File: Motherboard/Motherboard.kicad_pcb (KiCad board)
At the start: 4 copper layers, 246.4 x 175.3 mm, 57 parts, among them J1 40-pin IDE Connector, J3 Bus_ISA_8bit, J4 ATX-24, J5 USB_B, J6 ATF15XX_JTAG_ISP, J7 Bus_ISA_8bit, J8 65SIB_Connector, SW1 SW_Push, SW2 SW_SPST, U1 AS6C8008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

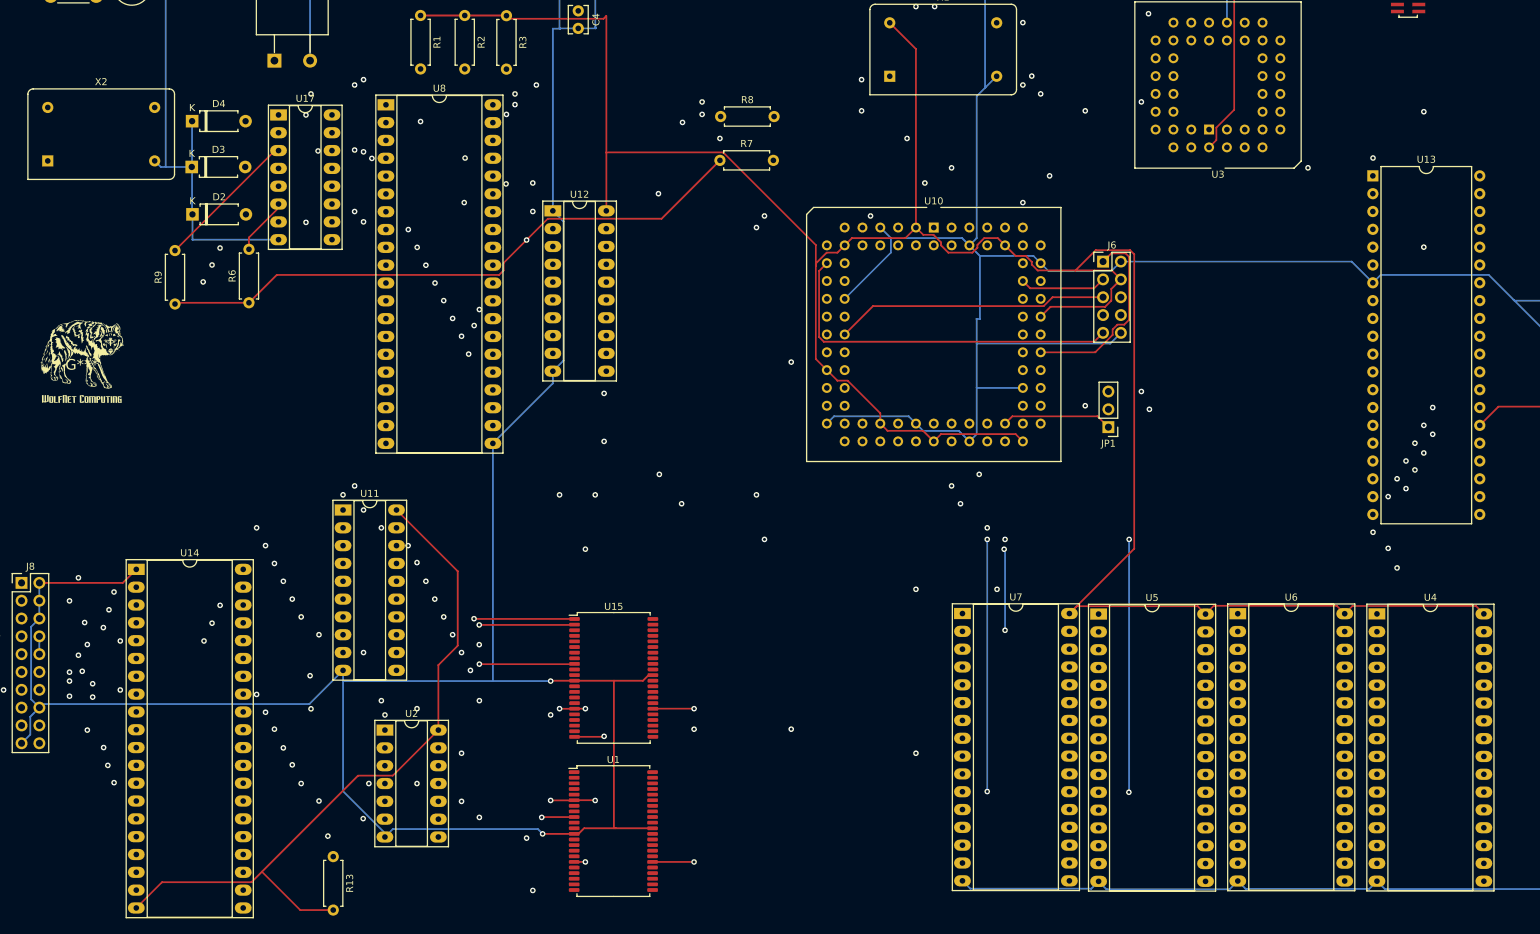
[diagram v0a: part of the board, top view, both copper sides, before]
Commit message: 230 unrouted traces...
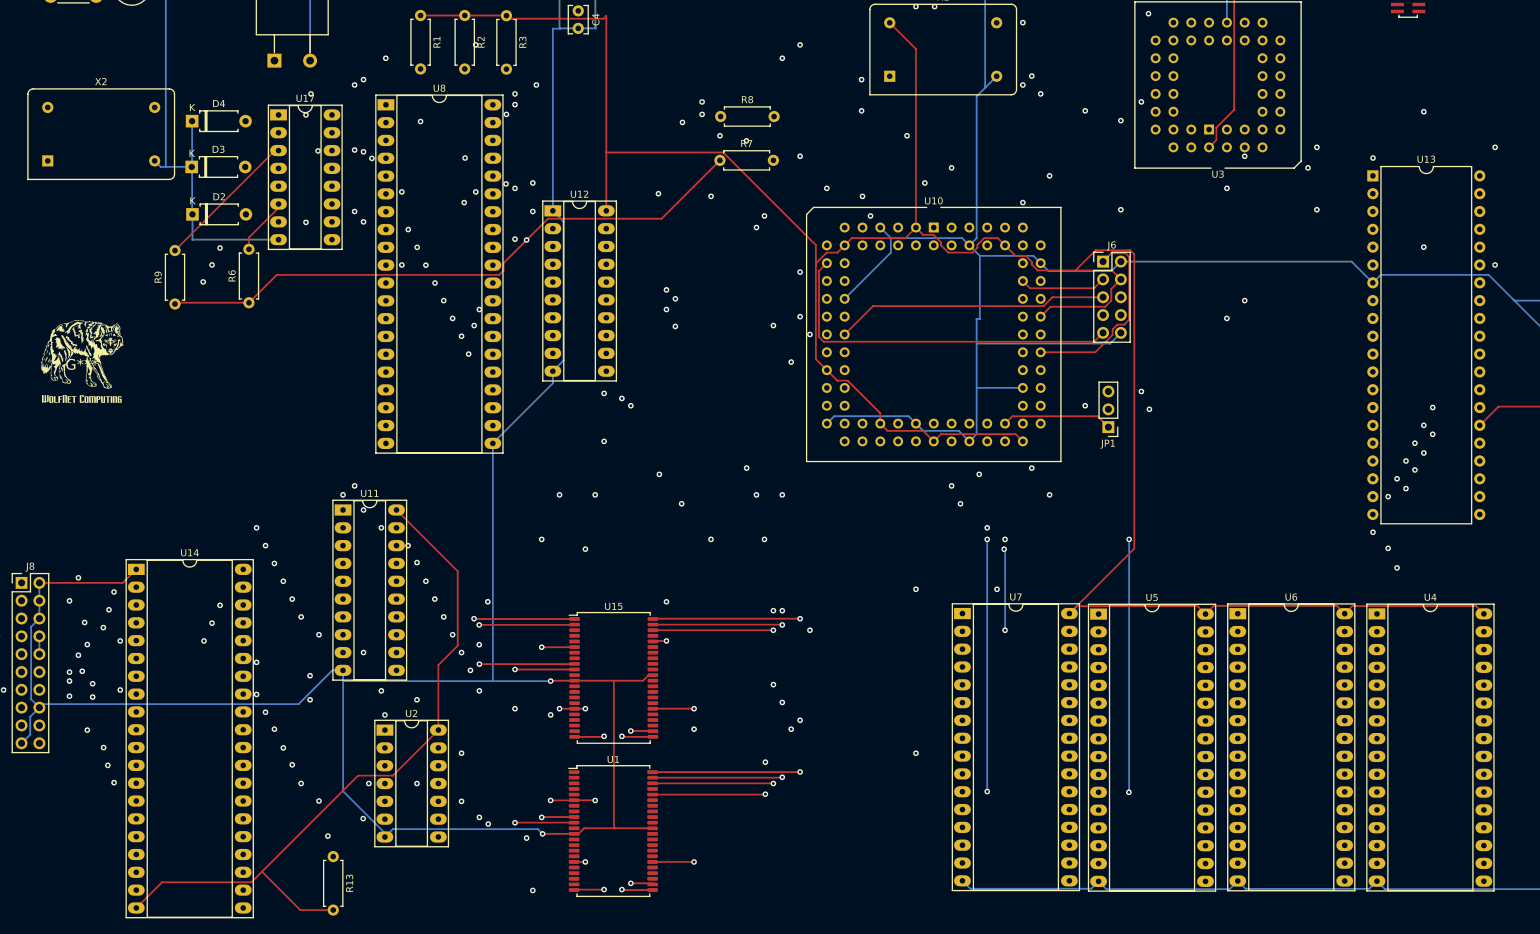
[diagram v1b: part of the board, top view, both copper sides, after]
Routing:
- net A1: track 142.2 -> 375.3 mm, vias 2 -> 11
- net A0: track 141.6 -> 323.3 mm, vias 2 -> 7
- net ~{VectorPull}: track 0.00 -> 174.2 mm, vias 0 -> 4
- net A6: track 62.1 -> 201.1 mm, vias 0 -> 6
- net A5: track 62.1 -> 196.0 mm, vias 0 -> 4
- net A7: track 62.3 -> 195.3 mm, vias 0 -> 5
- net Memory/IndexSelect: track 0.00 -> 130.4 mm, vias 0 -> 3
- net ~{RAM1_EN}: track 0.00 -> 119.1 mm, vias 0 -> 5
- net RESET: track 134.1 -> 236.0 mm, vias 5 -> 11
- net Net-(U15-CE2): track 0.00 -> 80.1 mm, vias 0 -> 4
- net A14: track 113.7 -> 192.5 mm, vias 0 -> 3
- net Net-(U1-CE2): track 0.00 -> 75.7 mm, vias 0 -> 2
- net D1: track 99.9 -> 174.4 mm, vias 2 -> 5
- net A13: track 109.9 -> 184.3 mm, vias 0 -> 3
- net A3: track 171.5 -> 226.9 mm, vias 3 -> 5
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
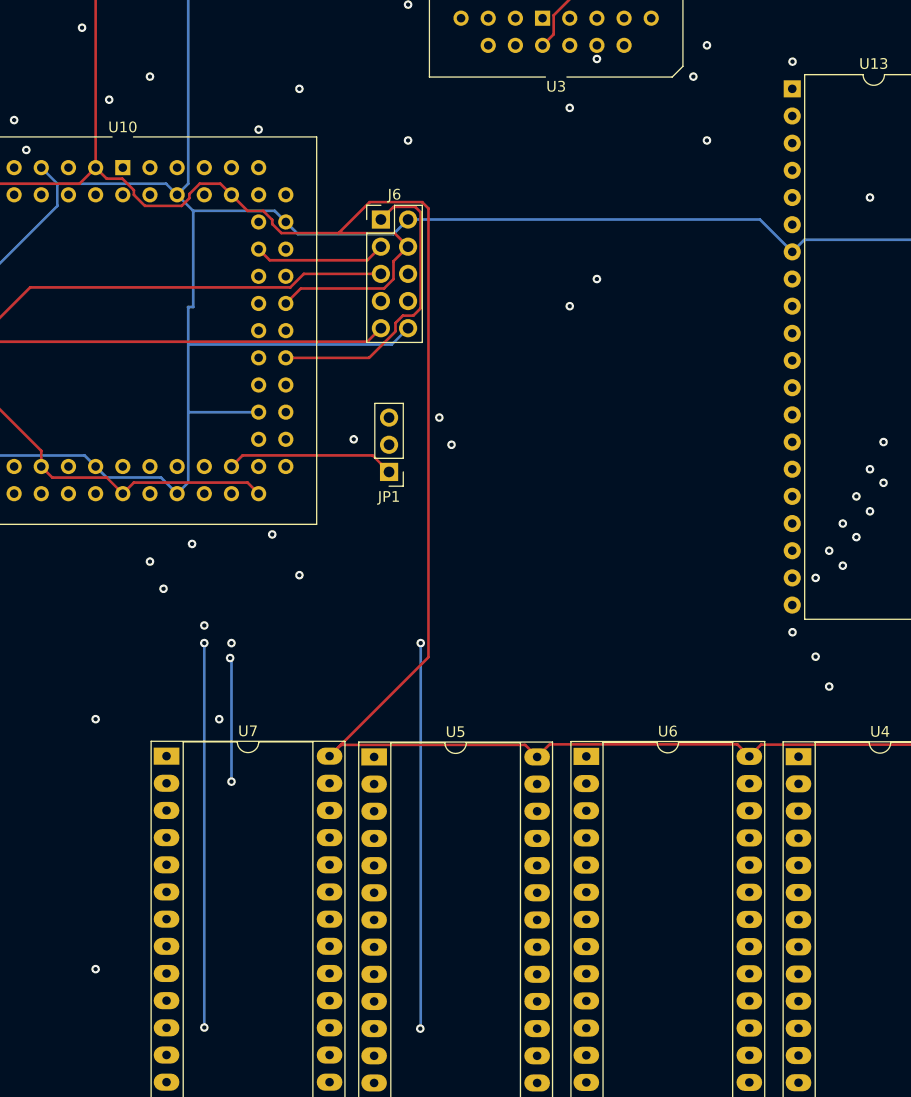
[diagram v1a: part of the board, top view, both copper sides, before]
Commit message: 226 unrouted traces...
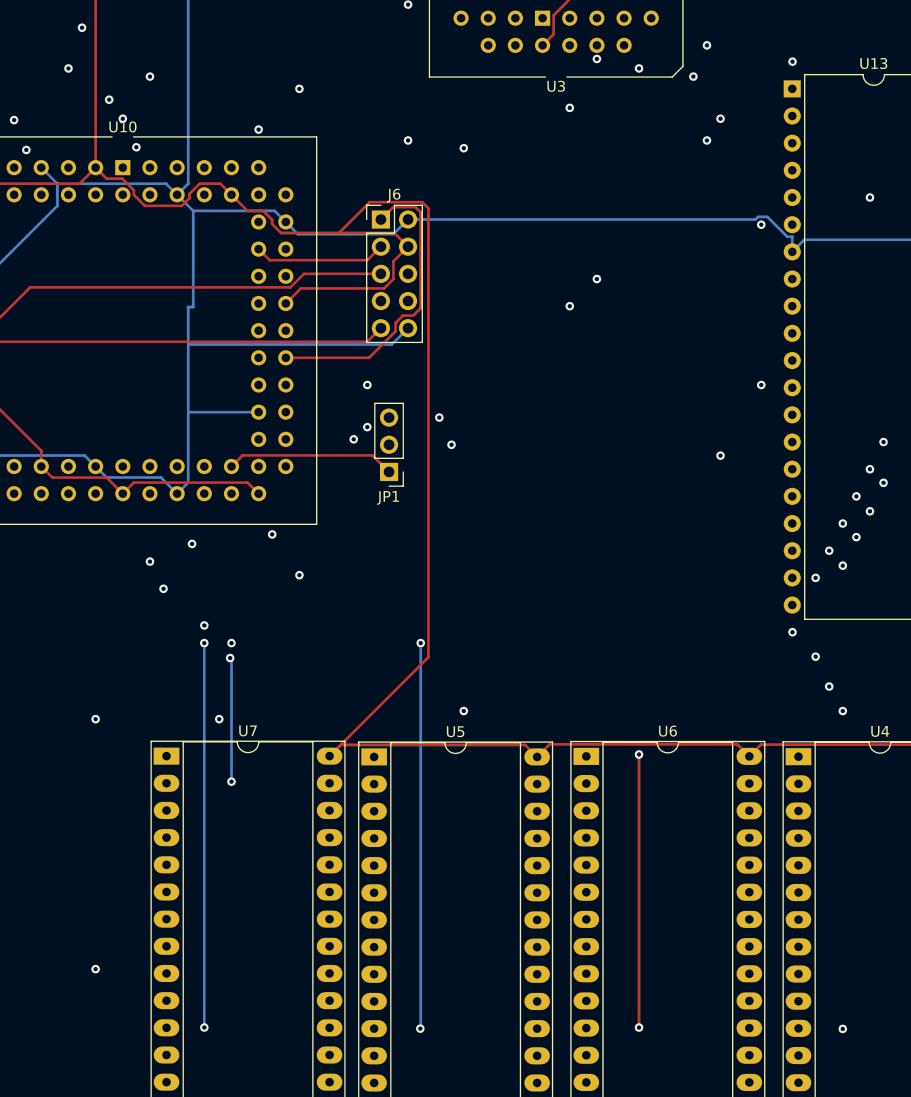
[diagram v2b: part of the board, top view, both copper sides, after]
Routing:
- net ~{FLASH1_EN}: track 0.00 -> 164.5 mm, vias 0 -> 5
- net ~{FLASH3_EN}: track 0.00 -> 162.6 mm, vias 0 -> 4
- net ~{RESET}: track 358.7 -> 487.5 mm, vias 13 -> 16
- net ~{IDE_EN}: track 0.00 -> 69.3 mm, vias 0 -> 4
- net GND: track 1295.9 -> 1296.9 mm

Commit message: 222 unrouted traces...
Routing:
- net IRQ: track 0.00 -> 236.2 mm, vias 0 -> 4
- net ~{DRQ3}: track 0.00 -> 116.6 mm, vias 0 -> 4
- net ~{IDE_READ}: track 0.00 -> 73.3 mm, vias 0 -> 4
- net ~{RAM1_EN}: track 119.1 -> 162.7 mm, vias 5 -> 6
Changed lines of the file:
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@@
   (segment (start 308.615 127.259) (end 308.61 127.254) (width 0.25) (layer "In2.Cu") (net 13))
   (segment (start 308.61 185.674) (end 312.6994 185.674) (width 0.25) (layer "In2.Cu") (net 13))
+  (via (at 317.5 129.794) (size 0.8) (drill 0.4) (layers "F.Cu" "B.Cu") (net 14))
+  (via (at 317.5 144.78) (size 0.8) (drill 0.4) (layers "F.Cu" "B.Cu") (net 14))
+  (via (at 309.88 144.78) (size 0.8) (drill 0.4) (layers "F.Cu" "B.Cu") (net 14))
+  (via (at 309.88 188.214) (size 0.8) (drill 0.4) (layers "F.Cu" "B.Cu") (net 14))
+  (segment (start 309.88 144.78) (end 309.88 188.214) (width 0.25) (layer "In1.Cu") (net 14))
+  (segment (start 317.5 129.794) (end 317.5 144.78) (width 0.25) (layer "In1.Cu") (net 14))
+  (segment (start 309.88 188.214) (end 312.6994 188.214) (width 0.25) (layer "In2.Cu") (net 14))
+  (segment (start 317.5 144.78) (end 309.88 144.78) (width 0.25) (layer "In2.Cu") (net 14))
+  (segment (start 317.495 129.799) (end 317.5 129.794) (width 0.25) (layer "In2.Cu") (net 14))
+  (segment (start 313.065 129.799) (end 317.495 129.799) (width 0.25) (layer "In2.Cu") (net 14))
   (via (at 133.35 166.37) (size 0.8) (drill 0.4) (layers "F.Cu" "B.Cu") (net 16))
   (via (at 218.44 166.37) (size 0.8) (drill 0.4) (layers "F.Cu" "B.Cu") (net 16))
@@
   (segment (start 318.77 117.094) (end 318.77 155.067) (width 0.25) (layer "B.Cu") (net 29))
   (segment (start 318.77 67.31) (end 318.77 69.85) (width 0.25) (layer "B.Cu") (net 29))
+  (via (at 133.35 227.33) (size 0.8) (drill 0.4) (layers "F.Cu" "B.Cu") (net 30))
+  (via (at 133.35 206.248) (size 0.8) (drill 0.4) (layers "F.Cu" "B.Cu") (net 30))
+  (via (at 309.88 227.33) (size 0.8) (drill 0.4) (layers "F.Cu" "B.Cu") (net 30))
+  (via (at 309.88 195.834) (size 0.8) (drill 0.4) (layers "F.Cu" "B.Cu") (net 30))
+  (segment (start 309.88 227.33) (end 309.88 195.834) (width 0.25) (layer "In1.Cu") (net 30))
+  (segment (start 133.35 206.248) (end 133.35 227.33) (width 0.25) (layer "In1.Cu") (net 30))
+  (segment (start 133.35 227.33) (end 309.88 227.33) (width 0.25) (layer "In2.Cu") (net 30))
+  (segment (start 137.668 206.248) (end 133.35 206.248) (width 0.25) (layer "In2.Cu") (net 30))
+  (segment (start 309.88 195.834) (end 312.6994 195.834) (width 0.25) (layer "In2.Cu") (net 30))
   (segment (start 290.8282 71.7532) (end 285.0408 71.7532) (width 0.25) (layer "F.Cu") (net 32))
   (segment (start 114.855 73.707) (end 114.808 73.66) (width 0.25) (layer "F.Cu") (net 32))
@@
   (segment (start 114.808 73.66) (end 252.73 73.66) (width 0.25) (layer "In2.Cu") (net 32))
   (segment (start 312.6994 170.434) (end 293.7256 170.434) (width 0.25) (layer "In2.Cu") (net 33))
+  (via (at 248.92 181.61) (size 0.8) (drill 0.4) (layers "F.Cu" "B.Cu") (net 39))
+  (via (at 248.92 151.13) (size 0.8) (drill 0.4) (layers "F.Cu" "B.Cu") (net 39))
+  (via (at 297.18 181.61) (size 0.8) (drill 0.4) (layers "F.Cu" "B.Cu") (net 39))
+  (via (at 297.18 183.134) (size 0.8) (drill 0.4) (layers "F.Cu" "B.Cu") (net 39))
+  (segment (start 297.18 181.61) (end 297.18 183.134) (width 0.25) (layer "In1.Cu") (net 39))
+  (segment (start 248.92 151.13) (end 248.92 181.61) (width 0.25) (layer "In1.Cu") (net 39))
+  (segment (start 248.92 181.61) (end 297.18 181.61) (width 0.25) (layer "In2.Cu") (net 39))
+  (segment (start 297.18 183.134) (end 312.6994 183.134) (width 0.25) (layer "In2.Cu") (net 39))
+  (segment (start 229.87 151.13) (end 248.92 151.13) (width 0.25) (layer "In2.Cu") (net 39))
+  (segment (start 228.6 149.86) (end 229.87 151.13) (width 0.25) (layer "In2.Cu") (net 39))
   (segment (start 281.9908 77.7532) (end 269.3378 77.7532) (width 0.25) (layer "F.Cu") (net 42))
   (segment (start 269.3378 77.7532) (end 269.24 77.851) (width 0.25) (layer "F.Cu") (net 42))
@@
   (segment (start 168.91 202.057) (end 168.91 223.901) (width 0.25) (layer "In1.Cu") (net 62))
   (segment (start 240.52 190.8376) (end 258.0566 190.8376) (width 0.25) (layer "In1.Cu") (net 62))
-  (segment (start 155.946 153.035) (end 153.0554 150.1444) (width 0.25) (layer "In2.Cu") (net 62))
-  (segment (start 168.7657 153.035) (end 155.946 153.035) (width 0.25) (layer "In2.Cu") (net 62))
+  (segment (start 168.7657 153.035) (end 162.052 153.035) (width 0.25) (layer "In2.Cu") (net 62))
+  (segment (start 162.052 153.035) (end 159.1614 150.1444) (width 0.25) (layer "In2.Cu") (net 62))
+  (segment (start 159.1614 150.1444) (end 153.0554 150.1444) (width 0.25) (layer "In2.Cu") (net 62))
   (segment (start 168.91 153.1793) (end 168.7657 153.035) (width 0.25) (layer "In2.Cu") (net 62))
   (segment (start 168.91 160.02) (end 203.2 160.02) (width 0.25) (layer "In2.Cu") (net 62))
@@
   (segment (start 164.6702 189.357) (end 164.6946 189.3326) (width 0.25) (layer "F.Cu") (net 149))
   (segment (start 160.02 189.357) (end 164.6702 189.357) (width 0.25) (layer "F.Cu") (net 149))
+  (via (at 160.02 210.058) (size 0.8) (drill 0.4) (layers "F.Cu" "B.Cu") (net 149))
   (via (at 160.02 173.99) (size 0.8) (drill 0.4) (layers "F.Cu" "B.Cu") (net 149))
   (via (at 160.02 189.357) (size 0.8) (drill 0.4) (layers "F.Cu" "B.Cu") (net 149))
@@
   (via (at 205.74 125.095) (size 0.8) (drill 0.4) (layers "F.Cu" "B.Cu") (net 149))
   (via (at 184.15 125.095) (size 0.8) (drill 0.4) (layers "F.Cu" "B.Cu") (net 149))
+  (segment (start 160.02 210.058) (end 160.02 189.357) (width 0.25) (layer "In1.Cu") (net 149))
   (segment (start 205.74 129.54) (end 205.74 125.095) (width 0.25) (layer "In1.Cu") (net 149))
   (segment (start 184.15 125.095) (end 184.15 173.99) (width 0.25) (layer "In1.Cu") (net 149))
   (segment (start 160.02 173.99) (end 160.02 189.357) (width 0.25) (layer "In1.Cu") (net 149))
   (segment (start 184.15 173.99) (end 160.02 173.99) (width 0.25) (layer "In2.Cu") (net 149))
+  (segment (start 137.668 211.328) (end 138.938 210.058) (width 0.25) (layer "In2.Cu") (net 149))
+  (segment (start 138.938 210.058) (end 160.02 210.058) (width 0.25) (layer "In2.Cu") (net 149))
   (segment (start 205.74 125.095) (end 184.15 125.095) (width 0.25) (layer "In2.Cu") (net 149))
   (segment (start 312.6994 205.994) (end 312.6994 211.8106) (width 0.25) (layer "In1.Cu") (net 151))

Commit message: 200 unrouted traces...
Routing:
- net ~{65SIB_EN}: track 0.00 -> 205.4 mm, vias 0 -> 5
- net ~{DACK3}: track 0.00 -> 137.3 mm, vias 0 -> 4
- net IO_RDY: track 0.00 -> 124.2 mm, vias 0 -> 5
- net A12: track 62.6 -> 171.4 mm, vias 0 -> 3
- net D3: track 99.9 -> 196.5 mm, vias 2 -> 4
- net A4: track 185.2 -> 280.4 mm, vias 4 -> 9
- net D0: track 223.3 -> 315.7 mm, vias 9 -> 11
- net D1: track 174.4 -> 266.8 mm, vias 5 -> 7
- net D2: track 99.7 -> 192.1 mm, vias 2 -> 4
- net D4: track 99.8 -> 188.9 mm, vias 2 -> 4
- net D5: track 100.2 -> 181.7 mm, vias 2 -> 4
- net A14: track 192.5 -> 268.1 mm, vias 3 -> 6
- net D6: track 101.3 -> 175.1 mm, vias 2 -> 4
- net A8: track 62.2 -> 131.4 mm, vias 0 -> 2
- net D7: track 105.9 -> 172.2 mm, vias 2 -> 4
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
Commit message: 190 unrouted traces...
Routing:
- net D0: track 315.7 -> 429.7 mm, vias 11 -> 17
- net D4: track 188.9 -> 298.8 mm, vias 4 -> 8
- net D6: track 175.1 -> 284.1 mm, vias 4 -> 8
- net D5: track 181.7 -> 279.6 mm, vias 4 -> 8
- net D7: track 172.2 -> 262.1 mm, vias 4 -> 5
- net D3: track 196.5 -> 279.0 mm, vias 4 -> 9
- net D1: track 266.8 -> 335.8 mm, vias 7 -> 11
- net D2: track 192.1 -> 237.0 mm, vias 4 -> 7
- net A12: track 171.4 -> 206.3 mm, vias 3 -> 4

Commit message: 180 unrouted traces...
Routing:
- net ~{65SIB_IRQ}: track 0.00 -> 237.6 mm, vias 0 -> 5
- net D7: track 262.1 -> 413.2 mm, vias 5 -> 10
- net A13: track 184.3 -> 273.8 mm, vias 3 -> 7
- net A17: track 123.2 -> 203.0 mm, vias 1 -> 6
- net A2: track 145.0 -> 208.9 mm, vias 2 -> 3
- net A18: track 102.7 -> 155.2 mm, vias 1 -> 5
- net A16: track 107.5 -> 151.3 mm, vias 1 -> 4
- net A3: track 226.9 -> 251.8 mm, vias 5 -> 7
- net -12V: track 396.0 -> 397.7 mm
- net +5V: track 951.7 -> 952.4 mm
- net A4: track 280.4 -> 281.2 mm
